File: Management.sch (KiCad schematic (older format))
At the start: 10 parts, among them J6 PDI, Q1 MMUN2231L, U1 ATXMEGA128A1U-AU, X1 16MHz, X2 32768

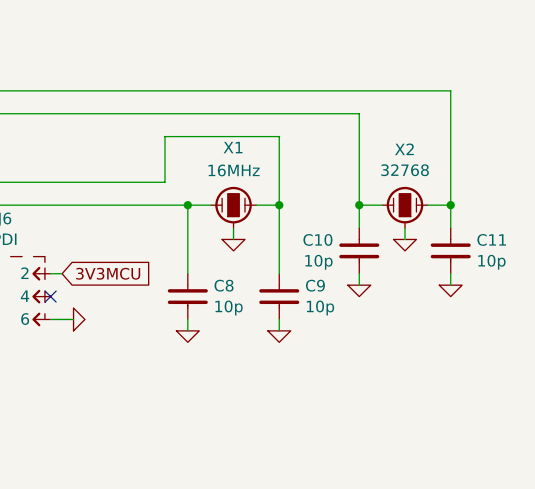
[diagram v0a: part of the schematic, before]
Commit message: Improved crystal layout
Shorter traces, less coupling between RAM bus and TOSC
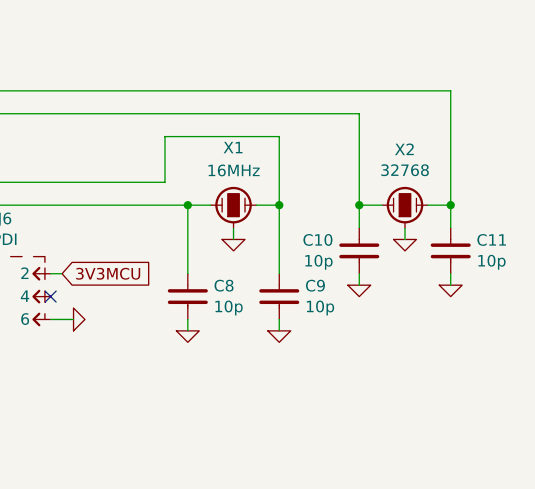
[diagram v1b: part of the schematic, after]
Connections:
- net TOSC1: now also X2.2; no longer X2.1
- net TOSC2: now also X2.1; no longer X2.2
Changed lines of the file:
@@
 F 4 "DIST DIGIKEY 300-8039-1-ND" H 7200 3400 60  0001 C CNN "BOM"
 	1    7200 3400
-	0    1    -1   0
+	0    -1   -1   0
 $EndComp
 $Comp
